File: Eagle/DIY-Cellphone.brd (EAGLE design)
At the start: 130.8 x 58.4 mm, 64 parts, among them IC1 MEGA1284, J1 ISP, U1 MCP73831, U7 M10_HDWITHOUT_EXCLUSION, X1 BU-SMA-V, X3 CCM03-3002 R102

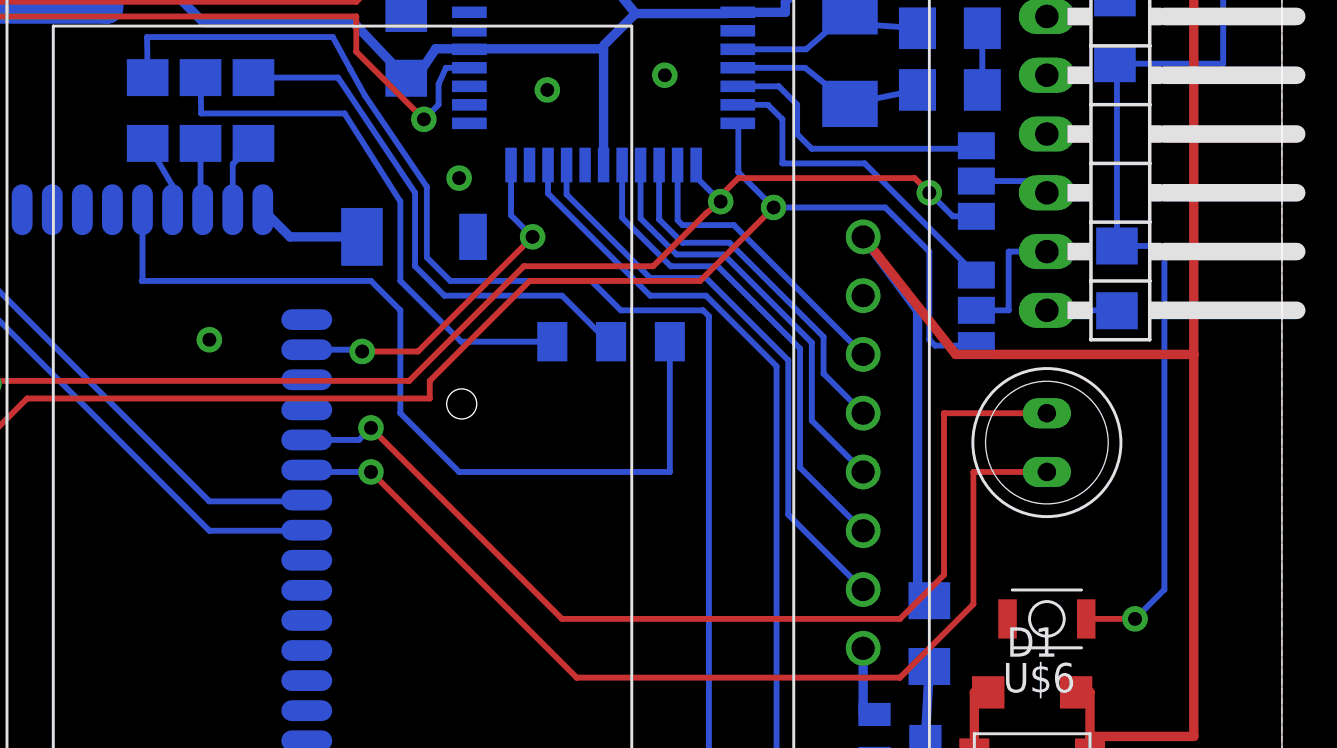
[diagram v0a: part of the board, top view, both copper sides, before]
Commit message: New supercap.
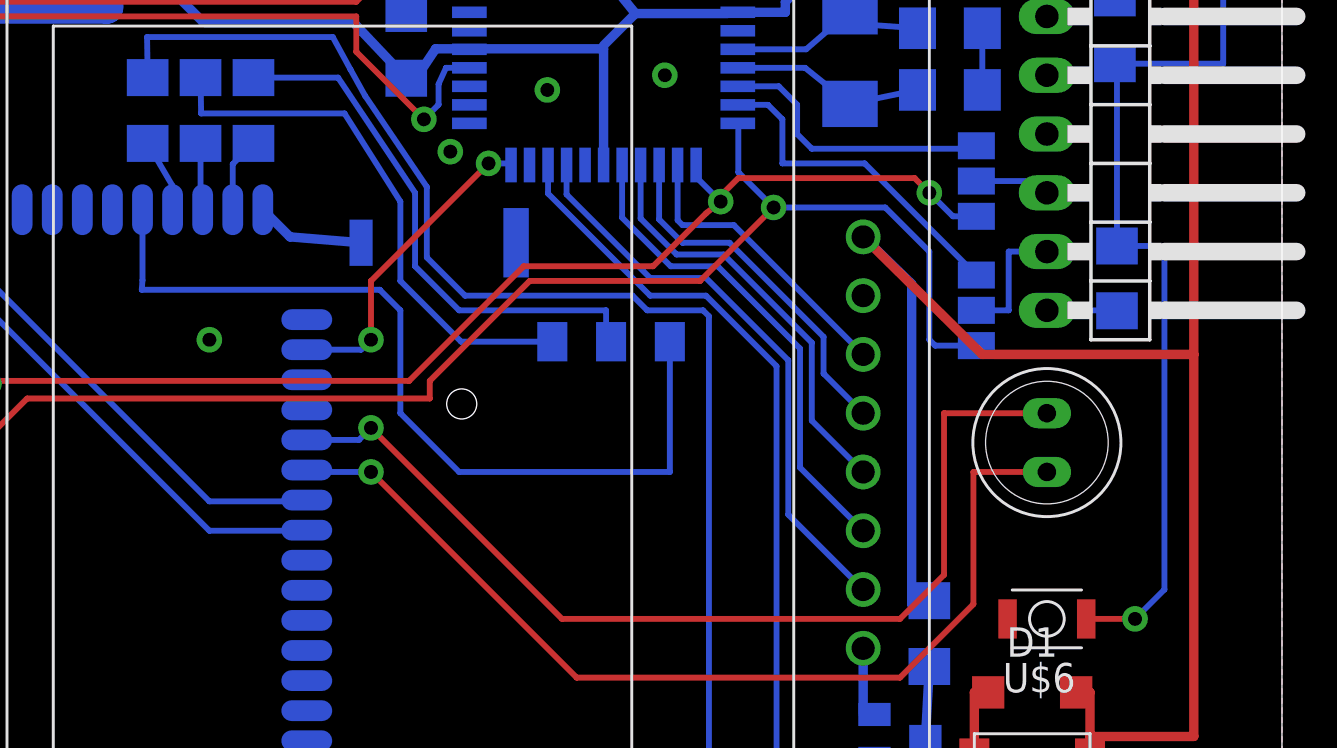
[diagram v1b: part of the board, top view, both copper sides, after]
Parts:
- U$4: value SUPERCAP -> SUPERCAPPAS; device cellphone:EP-A -> cellphone:414-VA5R
- moved U$4 0.92 mm to (94.4, 37.8), turned to 180 degrees
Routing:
- net PWRKEY: track 15.3 -> 13.7 mm
- net SIM_RSTR: track 22.6 -> 23.4 mm
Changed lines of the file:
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@@
 <setting verticaltext="up"/>
 </settings>
-<grid distance="25" unitdist="mil" unit="mm" style="dots" multiple="2" display="no" altdistance="5" altunitdist="mil" altunit="mil"/>
+<grid distance="25" unitdist="mil" unit="mil" style="dots" multiple="2" display="no" altdistance="5" altunitdist="mil" altunit="mil"/>
 <layers>
 <layer number="1" name="Top" color="4" fill="1" visible="yes" active="yes"/>
@@
 <attribute name="VALUE" x="113.03" y="19.685" size="1.27" layer="28" rot="MR90"/>
 </element>
-<element name="U$4" library="cellphone" package="EP-A" value="SUPERCAP" x="95.25" y="38.1" rot="MR270"/>
+<element name="U$4" library="cellphone" package="414-VA5R" value="SUPERCAPPAS" x="94.361" y="37.846" rot="MR180"/>
 <element name="8MHZ" library="fab" package="2-SMD-5X3MM" value="CRYSTAL" x="112.141" y="45.847" smashed="yes" rot="MR90">
 <attribute name="NAME" x="114.808" y="41.021" size="1.016" layer="26" rot="MR0"/>
@@
 <wire x1="54.61" y1="41.91" x2="54.61" y2="20.32" width="1.4224" layer="16"/>
 <wire x1="127" y1="49.53" x2="127" y2="33.02" width="0.4064" layer="1"/>
-<wire x1="127" y1="33.02" x2="116.713" y2="33.02" width="0.4064" layer="1"/>
-<wire x1="116.713" y1="33.02" x2="112.71" y2="38.1" width="0.4064" layer="1"/>
+<wire x1="127" y1="33.02" x2="117.856" y2="33.02" width="0.4064" layer="1"/>
+<wire x1="117.856" y1="33.02" x2="112.71" y2="38.1" width="0.4064" layer="1"/>
 <wire x1="100.692" y1="52.806" x2="100.692" y2="50.438" width="0.4064" layer="16"/>
 <wire x1="100.692" y1="50.438" x2="102.87" y2="47.752" width="0.4064" layer="16"/>
@@
 <wire x1="127" y1="33.02" x2="127" y2="16.51" width="0.4064" layer="1"/>
 <wire x1="115.57" y1="22.377" x2="114.935" y2="22.86" width="0.4064" layer="16"/>
-<wire x1="114.935" y1="22.86" x2="115.062" y2="22.225" width="0.4064" layer="16"/>
-<wire x1="115.062" y1="22.225" x2="115.062" y2="34.925" width="0.4064" layer="16"/>
-<wire x1="115.062" y1="34.925" x2="112.71" y2="38.1" width="0.4064" layer="16"/>
+<wire x1="114.935" y1="22.86" x2="114.808" y2="22.225" width="0.4064" layer="16"/>
+<wire x1="114.808" y1="22.225" x2="114.808" y2="36.068" width="0.4064" layer="16"/>
+<wire x1="114.808" y1="36.068" x2="112.71" y2="38.1" width="0.4064" layer="16"/>
 <wire x1="80.01" y1="49.53" x2="82.042" y2="49.53" width="0.4064" layer="16"/>
 <wire x1="82.042" y1="49.53" x2="84.201" y2="47.371" width="0.4064" layer="16"/>
@@
 <wire x1="46.736" y1="32.893" x2="48.641" y2="32.893" width="1.524" layer="16"/>
 <via x="104.14" y="45.085" extent="1-16" drill="0.6"/>
-<via x="95.25" y="40.64" extent="1-16" drill="0.6"/>
+<via x="94.869" y="41.783" extent="1-16" drill="0.6"/>
 <via x="84.455" y="33.655" extent="1-16" drill="0.6"/>
 <wire x1="107.315" y1="10.16" x2="107.315" y2="10.795" width="0.254" layer="16"/>
@@
 <wire x1="95.25" y1="27.94" x2="92.71" y2="30.48" width="0.254" layer="16"/>
 <wire x1="92.71" y1="30.48" x2="92.71" y2="34.925" width="0.254" layer="16"/>
-<wire x1="92.71" y1="34.925" x2="91.44" y2="36.195" width="0.254" layer="16"/>
-<wire x1="91.44" y1="36.195" x2="81.534" y2="36.195" width="0.254" layer="16"/>
-<wire x1="81.534" y1="36.195" x2="81.565" y2="36.226" width="0.254" layer="16"/>
+<wire x1="92.71" y1="34.925" x2="91.821" y2="35.814" width="0.254" layer="16"/>
+<wire x1="91.821" y1="35.814" x2="81.534" y2="35.814" width="0.254" layer="16"/>
+<wire x1="81.534" y1="35.814" x2="81.565" y2="36.226" width="0.254" layer="16"/>
 <wire x1="81.565" y1="36.226" x2="81.565" y2="39.274" width="0.254" layer="16"/>
 </signal>
@@
 <contactref element="U$4" pad="+"/>
 <wire x1="86.765" y1="39.274" x2="87.939" y2="38.1" width="0.4064" layer="16"/>
-<wire x1="87.939" y1="38.1" x2="91.05" y2="38.1" width="0.4064" layer="16"/>
+<wire x1="87.939" y1="38.1" x2="91.011" y2="37.846" width="0.4064" layer="16"/>
 </signal>
 <signal name="DISP_CLK">
@@
 <contactref element="U7" pad="P$18"/>
 <contactref element="IC1" pad="22"/>
-<wire x1="97.492" y1="41.206" x2="97.492" y2="39.033" width="0.254" layer="16"/>
-<wire x1="97.492" y1="39.033" x2="98.425" y2="38.1" width="0.254" layer="16"/>
-<via x="98.425" y="38.1" extent="1-16" drill="0.6"/>
-<wire x1="98.425" y1="38.1" x2="93.472" y2="33.147" width="0.254" layer="1"/>
-<wire x1="93.472" y1="33.147" x2="91.059" y2="33.147" width="0.254" layer="1"/>
-<via x="91.059" y="33.147" extent="1-16" drill="0.6"/>
-<wire x1="91.059" y1="33.147" x2="90.982" y2="33.224" width="0.254" layer="16"/>
-<wire x1="90.982" y1="33.224" x2="88.665" y2="33.224" width="0.254" layer="16"/>
+<wire x1="88.665" y1="33.224" x2="91.009" y2="33.224" width="0.254" layer="16"/>
+<wire x1="91.009" y1="33.224" x2="91.44" y2="33.655" width="0.254" layer="16"/>
+<via x="91.44" y="33.655" extent="1-16" drill="0.6"/>
+<wire x1="91.44" y1="33.655" x2="91.44" y2="36.195" width="0.254" layer="1"/>
+<wire x1="91.44" y1="36.195" x2="96.52" y2="41.275" width="0.254" layer="1"/>
+<via x="96.52" y="41.275" extent="1-16" drill="0.6"/>
+<wire x1="96.52" y1="41.275" x2="97.423" y2="41.275" width="0.254" layer="16"/>
+<wire x1="97.423" y1="41.275" x2="97.492" y2="41.206" width="0.254" layer="16"/>
 </signal>
 <signal name="SPK2P">
@@
 <wire x1="90.018" y1="44.983" x2="93.345" y2="40.005" width="0.254" layer="16"/>
 <wire x1="93.345" y1="40.005" x2="93.345" y2="36.83" width="0.254" layer="16"/>
-<wire x1="93.345" y1="36.83" x2="94.615" y2="35.56" width="0.254" layer="16"/>
-<wire x1="94.615" y1="35.56" x2="99.695" y2="35.56" width="0.254" layer="16"/>
-<wire x1="99.695" y1="35.56" x2="101.6" y2="33.655" width="0.254" layer="16"/>
+<wire x1="93.345" y1="36.83" x2="95.25" y2="34.925" width="0.254" layer="16"/>
+<wire x1="95.25" y1="34.925" x2="101.6" y2="34.925" width="0.254" layer="16"/>
+<wire x1="101.6" y1="34.925" x2="101.6" y2="33.655" width="0.254" layer="16"/>
 <wire x1="101.816" y1="33.57" x2="101.731" y2="33.655" width="0.254" layer="16"/>
 <wire x1="101.731" y1="33.655" x2="101.6" y2="33.655" width="0.254" layer="16"/>
@@
 <wire x1="91.186" y1="44.196" x2="93.853" y2="40.259" width="0.254" layer="16"/>
 <wire x1="93.853" y1="40.259" x2="93.853" y2="37.211" width="0.254" layer="16"/>
-<wire x1="102.235" y1="34.925" x2="105.791" y2="34.925" width="0.254" layer="16"/>
+<wire x1="103.378" y1="34.925" x2="105.791" y2="34.925" width="0.254" layer="16"/>
 <wire x1="105.791" y1="34.925" x2="106.045" y2="34.671" width="0.254" layer="16"/>
 <wire x1="106.045" y1="34.671" x2="106.045" y2="15.24" width="0.254" layer="16"/>
 <wire x1="106.045" y1="15.24" x2="99.276" y2="8.471" width="0.254" layer="16"/>
 <wire x1="99.276" y1="8.471" x2="99.276" y2="7.87" width="0.254" layer="16"/>
-<wire x1="93.853" y1="37.211" x2="94.869" y2="36.195" width="0.254" layer="16"/>
-<wire x1="94.869" y1="36.195" x2="100.965" y2="36.195" width="0.254" layer="16"/>
-<wire x1="100.965" y1="36.195" x2="102.235" y2="34.925" width="0.254" layer="16"/>
+<wire x1="93.853" y1="37.211" x2="95.504" y2="35.56" width="0.254" layer="16"/>
+<wire x1="95.504" y1="35.56" x2="102.743" y2="35.56" width="0.254" layer="16"/>
+<wire x1="102.743" y1="35.56" x2="103.378" y2="34.925" width="0.254" layer="16"/>
 </signal>
 <signal name="RI">

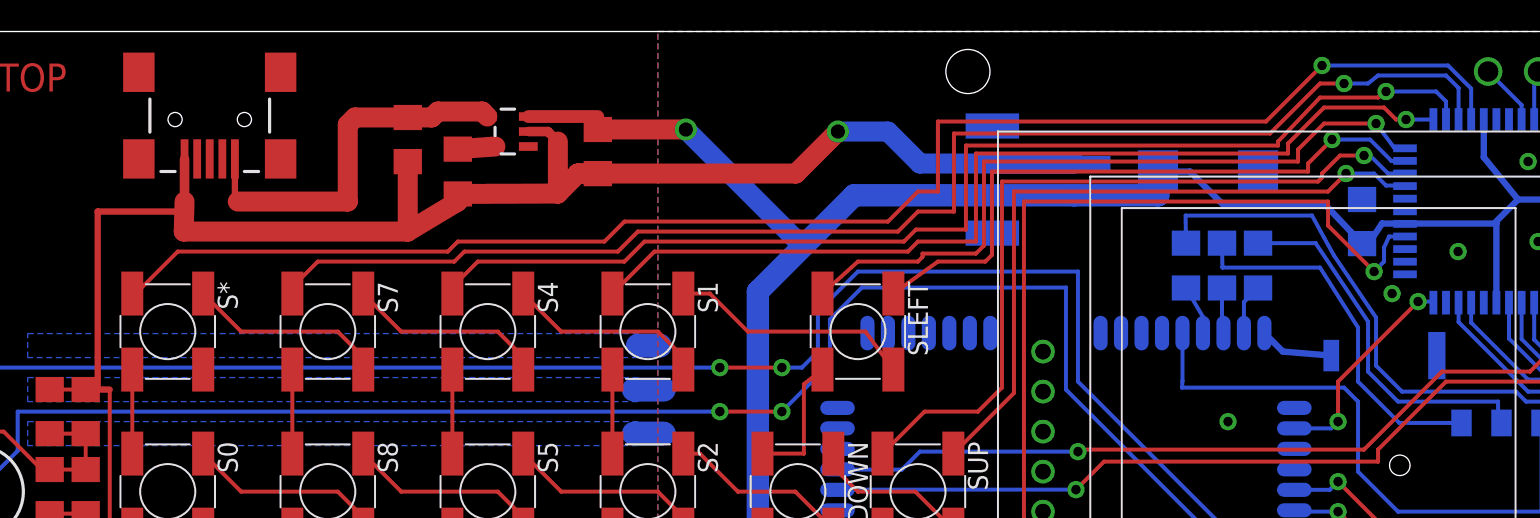
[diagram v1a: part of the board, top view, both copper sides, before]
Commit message: Adding heat dissipation and LED on charging circuit.
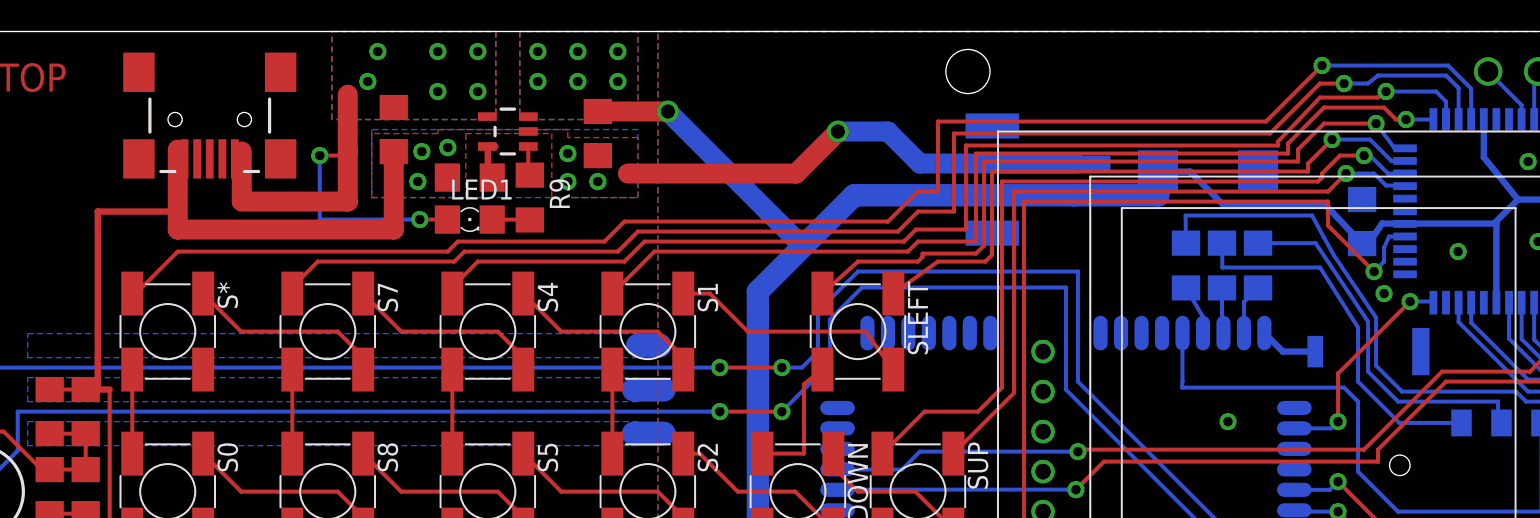
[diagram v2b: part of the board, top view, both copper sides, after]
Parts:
- added LED1: (no value), led:1206
- added R9: 470, rcl:R1206
- moved C4 1.14 mm to (44.5, 51.9)
- moved C3 1.09 mm to (31.5, 52.2)
- moved U$4 1.05 mm to (93.3, 38.1)
- moved R7 0.85 mm to (36.3, 49.1), turned to 180 degrees
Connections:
- new net N$35: R9.1, U1.1
- new net N$36: LED1.C, R9.2
- net VUSB: now also LED1.A
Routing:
- net GND: track 151.7 -> 133.5 mm, vias 28 -> 34
- net VUSB: track 24.0 -> 32.0 mm, vias 0 -> 8
- net VCC: track 243.7 -> 239.2 mm, vias 2 -> 8
- net N$36: track 0.00 -> 2.41 mm
- net N$35: track 0.00 -> 1.92 mm
- net VRTC: track 4.74 -> 3.72 mm
- added copper zone on layer 1, net VCC
- added copper zone on layer 16, net VCC
- added copper zone on layer 1, net VUSB
- added copper zone on layer 16, net VUSB
